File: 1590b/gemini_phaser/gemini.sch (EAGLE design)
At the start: 64 parts, among them IC1 TL074, IC2 TL072, Q1 2N5457, Q2 2N5457, Q3 2N5087, Q4 2N5457, Q5 J112, Q6 2N5457

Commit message: prettified schematics a bit
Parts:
- removed D4: LEDA, diodes:LEDA
- removed R2: 4k7, resistors:R_.3B
- added 9V: DC_MONO, jacks:DC_MONO
- added GND, PAD3: PADRND, supply pins:PADRND
- added IN, OUT: PADSQR, supply pins:PADSQR
- D2: value LEDA -> 5.1vZ; device diodes:LEDA -> diodes:ZENER.3
- D3: value 5.1vZ -> LEDA; device diodes:ZENER.3 -> diodes:LEDA
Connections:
- removed net +9V: D1.A
- removed net N$14: D2.A, R2.1
- new net LS: D3.C, PAD3.P$1
- new net N$34: 9V.TIP, D1.A
- net GND: now also 9V.SLEEVE, D2.A; no longer D2.C, D3.A, D4.C
- net IN: now also IN.P$1
- net N$17: now also D3.A; no longer D4.A
- net N$18: no longer R2.2
- net OUT: now also OUT.P$1
- net VA: now also D2.C; no longer D3.C
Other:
- moved on the sheet: BIAS, C1, C10, C12, C2, C3, C5, C6, C7, C8, D1, DEPTH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

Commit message: convert bitmap logos to polygons
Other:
- moved on the sheet: C4, IC2_A, R1, R3, R7
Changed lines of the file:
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@@
 <setting verticaltext="up"/>
 </settings>
-<grid distance="0.05" unitdist="inch" unit="inch" style="lines" multiple="2" display="no" altdistance="0.01" altunitdist="inch" altunit="inch"/>
+<grid distance="0.1" unitdist="inch" unit="inch" style="lines" multiple="1" display="no" altdistance="0.01" altunitdist="inch" altunit="inch"/>
 <layers>
 <layer number="1" name="Top" color="4" fill="1" visible="no" active="no"/>
@@
 </plain>
 <instances>
-<instance part="R3" gate="G$1" x="55.88" y="86.36"/>
-<instance part="C4" gate="G$1" x="68.58" y="86.36"/>
-<instance part="IC2" gate="_A" x="86.36" y="83.82"/>
+<instance part="R3" gate="G$1" x="53.34" y="86.36"/>
+<instance part="C4" gate="G$1" x="66.04" y="86.36"/>
+<instance part="IC2" gate="_A" x="83.82" y="83.82"/>
 <instance part="IC2" gate="_B" x="208.28" y="116.84" rot="R180"/>
 <instance part="IC2" gate="_PWR" x="55.88" y="127" rot="R180"/>
-<instance part="R7" gate="G$1" x="76.2" y="96.52" rot="R90"/>
+<instance part="R7" gate="G$1" x="73.66" y="96.52" rot="R90"/>
 <instance part="R10" gate="G$1" x="104.14" y="93.98"/>
 <instance part="MIX" gate="G$1" x="111.76" y="83.82" rot="MR180"/>
@@
 <instance part="GND3" gate="GND" x="38.1" y="116.84"/>
 <instance part="R31" gate="G$1" x="233.68" y="106.68" rot="R90"/>
-<instance part="R1" gate="G$1" x="45.72" y="78.74" rot="R90"/>
-<instance part="GND1" gate="GND" x="45.72" y="71.12"/>
+<instance part="R1" gate="G$1" x="43.18" y="78.74" rot="R90"/>
+<instance part="GND1" gate="GND" x="43.18" y="71.12"/>
 <instance part="MODE" gate="1" x="130.81" y="60.96" rot="R270"/>
 <instance part="DEPTH" gate="G$1" x="111.76" y="127" rot="MR90"/>
 <instance part="9V" gate="DC" x="17.78" y="132.08"/>
 <instance part="GND2" gate="GND" x="22.86" y="127"/>
-<instance part="IN" gate="G$1" x="38.1" y="86.36"/>
+<instance part="IN" gate="G$1" x="35.56" y="86.36"/>
 <instance part="OUT" gate="G$1" x="163.83" y="83.82"/>
 <instance part="PAD3" gate="G$1" x="134.62" y="127"/>
@@
 <segment>
 <pinref part="R3" gate="G$1" pin="2"/>
-<wire x1="60.96" y1="86.36" x2="64.77" y2="86.36" width="0.1524" layer="91"/>
+<wire x1="58.42" y1="86.36" x2="62.23" y2="86.36" width="0.1524" layer="91"/>
 <pinref part="C4" gate="G$1" pin="2"/>
 </segment>
@@
 <pinref part="IC2" gate="_A" pin="+IN"/>
 <pinref part="R7" gate="G$1" pin="1"/>
-<wire x1="72.39" y1="86.36" x2="76.2" y2="86.36" width="0.1524" layer="91"/>
-<wire x1="76.2" y1="86.36" x2="78.74" y2="86.36" width="0.1524" layer="91"/>
-<wire x1="76.2" y1="91.44" x2="76.2" y2="86.36" width="0.1524" layer="91"/>
-<junction x="76.2" y="86.36"/>
+<wire x1="69.85" y1="86.36" x2="73.66" y2="86.36" width="0.1524" layer="91"/>
+<wire x1="73.66" y1="86.36" x2="76.2" y2="86.36" width="0.1524" layer="91"/>
+<wire x1="73.66" y1="91.44" x2="73.66" y2="86.36" width="0.1524" layer="91"/>
+<junction x="73.66" y="86.36"/>
 <pinref part="C4" gate="G$1" pin="1"/>
 </segment>
@@
 <segment>
 <pinref part="IC2" gate="_A" pin="OUT"/>
-<wire x1="93.98" y1="83.82" x2="96.52" y2="83.82" width="0.1524" layer="91"/>
+<wire x1="91.44" y1="83.82" x2="96.52" y2="83.82" width="0.1524" layer="91"/>
 <wire x1="96.52" y1="83.82" x2="96.52" y2="93.98" width="0.1524" layer="91"/>
 <pinref part="R10" gate="G$1" pin="1"/>
@@
 <wire x1="55.88" y1="25.4" x2="59.69" y2="25.4" width="0.1524" layer="91"/>
 <pinref part="C2" gate="G$1" pin="2"/>
-<wire x1="96.52" y1="73.66" x2="76.2" y2="73.66" width="0.1524" layer="91"/>
-<wire x1="76.2" y1="73.66" x2="55.88" y2="73.66" width="0.1524" layer="91"/>
+<wire x1="96.52" y1="73.66" x2="73.66" y2="73.66" width="0.1524" layer="91"/>
+<wire x1="73.66" y1="73.66" x2="55.88" y2="73.66" width="0.1524" layer="91"/>
 <wire x1="55.88" y1="73.66" x2="55.88" y2="35.56" width="0.1524" layer="91"/>
 <junction x="55.88" y="35.56"/>
 <pinref part="IC2" gate="_A" pin="-IN"/>
-<wire x1="78.74" y1="81.28" x2="76.2" y2="81.28" width="0.1524" layer="91"/>
-<wire x1="76.2" y1="81.28" x2="76.2" y2="73.66" width="0.1524" layer="91"/>
-<junction x="76.2" y="73.66"/>
+<wire x1="76.2" y1="81.28" x2="73.66" y2="81.28" width="0.1524" layer="91"/>
+<wire x1="73.66" y1="81.28" x2="73.66" y2="73.66" width="0.1524" layer="91"/>
+<junction x="73.66" y="73.66"/>
 </segment>
 </net>
@@
 <segment>
 <pinref part="R3" gate="G$1" pin="1"/>
-<wire x1="35.56" y1="86.36" x2="38.1" y2="86.36" width="0.1524" layer="91"/>
+<wire x1="27.94" y1="86.36" x2="35.56" y2="86.36" width="0.1524" layer="91"/>
 <pinref part="R1" gate="G$1" pin="2"/>
-<wire x1="38.1" y1="86.36" x2="45.72" y2="86.36" width="0.1524" layer="91"/>
-<wire x1="45.72" y1="86.36" x2="50.8" y2="86.36" width="0.1524" layer="91"/>
-<wire x1="45.72" y1="83.82" x2="45.72" y2="86.36" width="0.1524" layer="91"/>
-<junction x="45.72" y="86.36"/>
-<label x="35.56" y="86.36" size="1.778" layer="95" rot="R180" xref="yes"/>
+<wire x1="35.56" y1="86.36" x2="43.18" y2="86.36" width="0.1524" layer="91"/>
+<wire x1="43.18" y1="86.36" x2="48.26" y2="86.36" width="0.1524" layer="91"/>
+<wire x1="43.18" y1="83.82" x2="43.18" y2="86.36" width="0.1524" layer="91"/>
+<junction x="43.18" y="86.36"/>
+<label x="27.94" y="86.36" size="1.778" layer="95" rot="R180" xref="yes"/>
 <pinref part="IN" gate="G$1" pin="P$1"/>
-<junction x="38.1" y="86.36"/>
+<junction x="35.56" y="86.36"/>
 </segment>
 </net>
@@
 <wire x1="153.67" y1="83.82" x2="154.94" y2="83.82" width="0.1524" layer="91"/>
 <wire x1="154.94" y1="83.82" x2="163.83" y2="83.82" width="0.1524" layer="91"/>
-<wire x1="163.83" y1="83.82" x2="166.37" y2="83.82" width="0.1524" layer="91"/>
+<wire x1="163.83" y1="83.82" x2="171.45" y2="83.82" width="0.1524" layer="91"/>
 <wire x1="154.94" y1="81.28" x2="154.94" y2="83.82" width="0.1524" layer="91"/>
 <junction x="154.94" y="83.82"/>
 <pinref part="C9" gate="G$1" pin="1"/>
-<label x="166.37" y="83.82" size="1.778" layer="95" xref="yes"/>
+<label x="171.45" y="83.82" size="1.778" layer="95" xref="yes"/>
 <pinref part="OUT" gate="G$1" pin="P$1"/>
 <junction x="163.83" y="83.82"/>
@@
 <segment>
 <pinref part="R7" gate="G$1" pin="2"/>
-<wire x1="76.2" y1="101.6" x2="76.2" y2="102.87" width="0.1524" layer="91"/>
-<label x="76.2" y="102.87" size="1.778" layer="95" rot="R90" xref="yes"/>
-</segment>
-<segment>
+<wire x1="73.66" y1="101.6" x2="73.66" y2="102.87" width="0.1524" layer="91"/>
+<label x="73.66" y="102.87" size="1.778" layer="95" rot="R90" xref="yes"/>
+</segment>
+<segment>

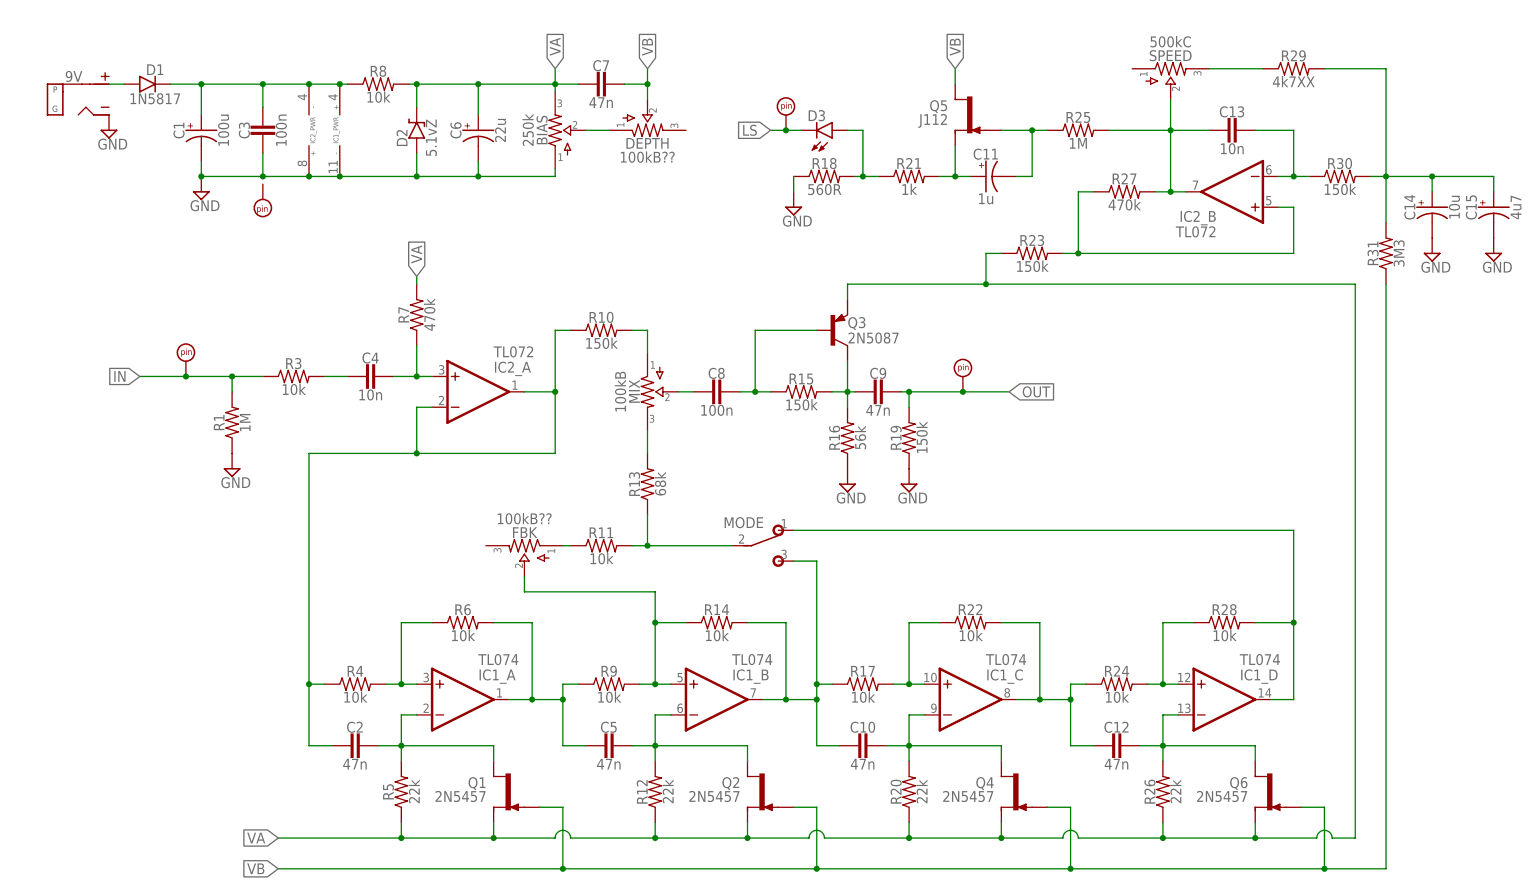
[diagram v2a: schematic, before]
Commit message: add SIREN build doc
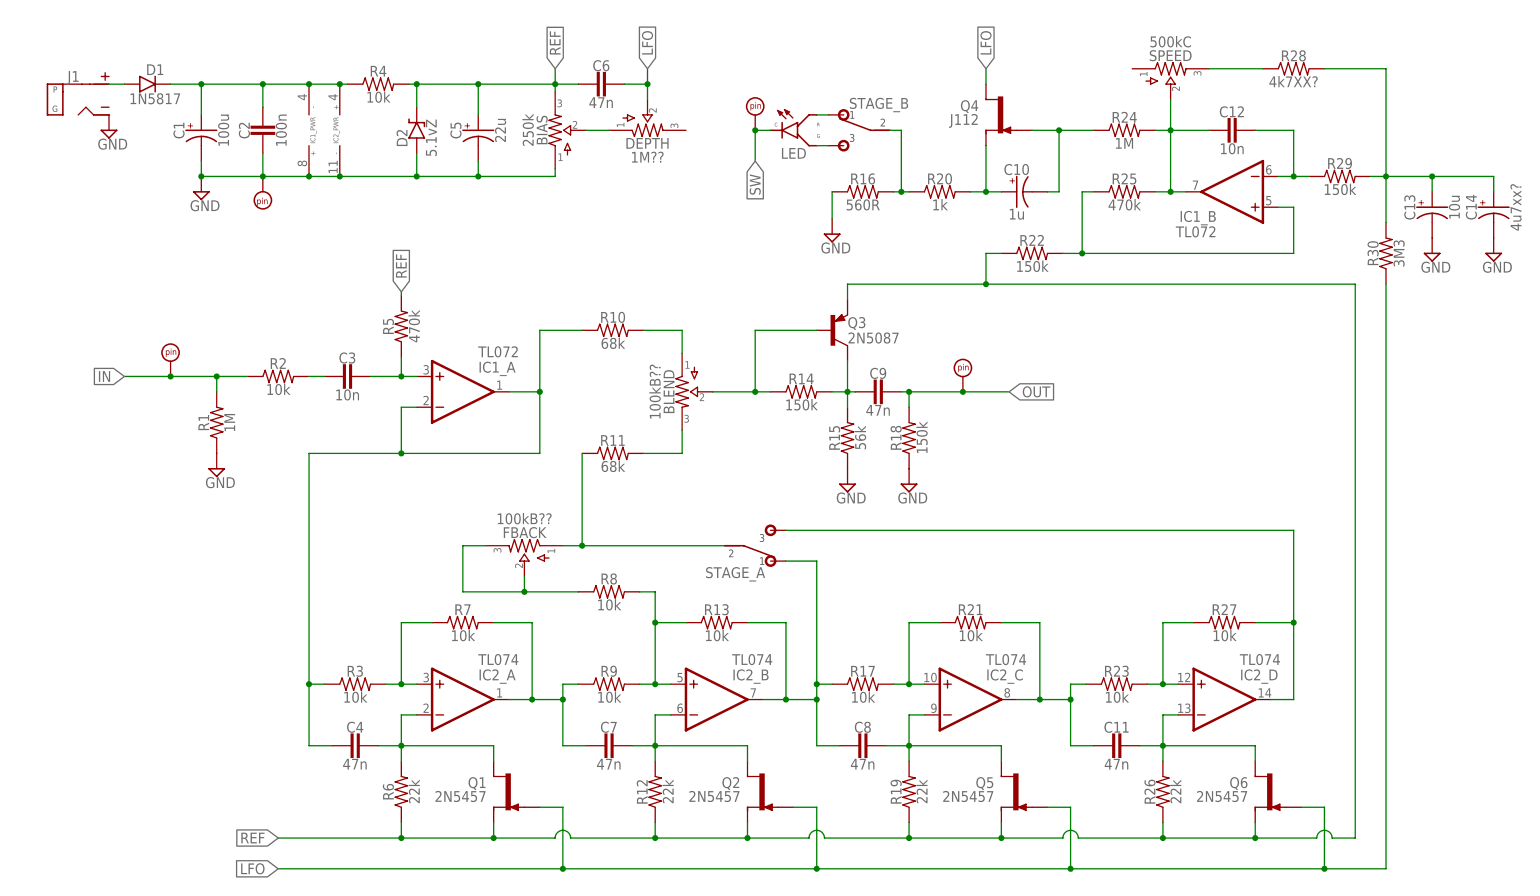
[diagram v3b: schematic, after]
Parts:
- removed C15: 4u7, capacitors-elec:0501
- removed D3: LEDA, diodes:LEDA
- removed GND: PADRND, supply pins:PADRND
- removed IN: PADSQR, supply pins:PADSQR
- removed MIX: 100kB, potentiometers:POTS16MM
- removed MODE: (no value), switches:SPDTPADS
- removed R31: 3M3, resistors:R_.3B
- added BLEND: 100kB??, potentiometers:POTS16MM
- added LED: LED_DUAL, diodes:LED_DUAL
- added PAD1: PADSQR, supply pins:PADSQR
- added PAD2: PADRND, supply pins:PADRND
- added R2: 10k, resistors:R_.3B
- added STAGE: (no value), switches:DPDTPCB
- C10: value 47n -> 1u; device capacitors-film:CER/FILM2 -> capacitors-elec:0501
- C11: value 1u -> 47n; device capacitors-elec:0501 -> capacitors-film:CER/FILM2
- C12: value 47n -> 10n
- C13: value 10n -> 10u; device capacitors-film:CER/FILM2 -> capacitors-elec:0501
- C14: value 10u -> 4u7xx?
- C2: value 47n -> 100n
- C3: value 100n -> 10n
- C4: value 10n -> 47n
- C5: value 47n -> 22u; device capacitors-film:CER/FILM2 -> capacitors-elec:0501
- C6: value 22u -> 47n; device capacitors-elec:0501 -> capacitors-film:CER/FILM2
- C8: value 100n -> 47n
- DEPTH: value 100kB?? -> 1M??
- IC1: value TL074 -> TL072; device integrated circuits:QUADTH -> integrated circuits:DUALTH
- IC2: value TL072 -> TL074; device integrated circuits:DUALTH -> integrated circuits:QUADTH
- Q4: value 2N5457 -> J112; device transistors:2N5457 -> transistors:J201
- Q5: value J112 -> 2N5457; device transistors:J201 -> transistors:2N5457
- R10: value 150k -> 68k
- R11: value 10k -> 68k
- R13: value 68k -> 10k
- R14, R22: value 10k -> 150k
- R15: value 150k -> 56k
- R16: value 56k -> 560R
- R18: value 560R -> 150k
- R19: value 150k -> 22k
- R20: value 22k -> 1k
- R21: value 1k -> 10k
- R23: value 150k -> 10k
- R24: value 10k -> 1M
- R25: value 1M -> 470k
- R27, R7: value 470k -> 10k
- R28: value 10k -> 4k7XX?
- R29: value 4k7XX -> 150k
- R30: value 150k -> 3M3
- R5: value 22k -> 470k
- R6: value 10k -> 22k
- renumbered 9V to J1, FBK to FBACK, OUT to PAD4
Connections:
- removed net LS: D3.C, PAD3.P$1
- removed net N$5: C8.2, MIX.2
- removed net VA: BIAS.3, C6.+, C7.2, D2.C, Q1.S, Q2.S, Q3.E, Q4.S, Q6.S, R12.1, R20.1, R23.1, R26.1, R5.1, R7.2, R8.2
- removed net VB: C7.1, DEPTH.2, Q1.G, Q2.G, Q4.G, Q5.D, Q6.G, R31.1
- new net LED: LED.G, STAGE_B.3
- new net LFO: C6.1, DEPTH.2, Q1.G, Q2.G, Q4.D, Q5.G, Q6.G, R30.1
- new net N$35: LED.R, STAGE_B.1
- new net REF: BIAS.3, C5.+, C6.2, D2.C, Q1.S, Q2.S, Q3.E, Q5.S, Q6.S, R12.1, R19.1, R22.1, R26.1, R4.2, R5.2, R6.1
- new net SW: LED.C, PAD3.P$1
- net GND: now also C13.-, C2.2, C5.-, IC1_PWR.V+, IC2_PWR.V-, PAD2.P$1, R15.1; no longer C15.-, C3.2, C6.-, IC1_PWR.V-, IC2_PWR.V+, R19.1
- net IN: now also PAD1.P$1, R2.1; no longer IN.P$1, R3.1
- net N$1: now also C3.2, R2.2; no longer C4.2, R3.2
- net N$10: now also IC1_B.+IN, R22.2, R25.1; no longer IC2_B.+IN, R23.2, R27.1
- net N$11: now also C12.2, IC1_B.OUT, R24.2; no longer C13.2, IC2_B.OUT, R27.2
- net N$12: now also R28.1; no longer R29.1
- net N$13: now also C12.1, IC1_B.-IN, R29.1; no longer C13.1, IC2_B.-IN, R30.1
- net N$15: now also C10.-, Q4.G, R24.1; no longer C11.-, Q5.G, R25.1
- net N$16: now also C10.+, Q4.S, R20.2; no longer C11.+, Q5.S, R21.2
- net N$17: now also R16.2, R20.1, STAGE_B.2; no longer D3.A, R18.2, R21.1
- net N$18: now also C2.1, IC1_PWR.V-, IC2_PWR.V+, R4.1; no longer C3.1, IC1_PWR.V+, IC2_PWR.V-, R8.1
- net N$19: now also BLEND.3, R11.2; no longer FBACK.1, R11.1
- net N$2: now also C3.1, IC1_A.+IN, R5.1; no longer C4.1, IC2_A.+IN, R7.1
- net N$20: now also IC2_B.+IN, R13.1, R8.2; no longer FBACK.2, IC1_B.+IN, R14.1
- net N$21: now also C4.1, IC2_A.-IN, R6.2; no longer C2.1, IC1_A.-IN, R5.2
- net N$22: now also IC2_A.+IN, R3.2, R7.1; no longer IC1_A.+IN, R4.2, R6.1
- net N$23: now also C7.2, IC2_A.OUT, R7.2; no longer C5.2, IC1_A.OUT, R6.2
- net N$24: now also C7.1, IC2_B.-IN; no longer C5.1, IC1_B.-IN
- net N$25: now also IC2_D.OUT, R27.2, STAGE_A.3; no longer IC1_D.OUT, MODE.O, R28.2
- net N$26: now also C8.2, IC2_B.OUT, R13.2, STAGE_A.1; no longer C10.2, IC1_B.OUT, MODE.S, R14.2
- net N$27: now also C8.1, IC2_C.-IN, Q5.D, R19.2; no longer C10.1, IC1_C.-IN, Q4.D, R20.2
- net N$28: now also IC2_C.+IN, R21.1; no longer IC1_C.+IN, R22.1
- net N$29: now also C11.2, IC2_C.OUT, R21.2, R23.1; no longer C12.2, IC1_C.OUT, R22.2, R24.1
- net N$3: now also C4.2, IC1_A.-IN, IC1_A.OUT, R3.1; no longer C2.2, IC2_A.-IN, IC2_A.OUT, R4.1
- net N$30: now also C11.1, IC2_D.-IN; no longer C12.1, IC1_D.-IN
- net N$31: now also IC2_D.+IN, R23.2, R27.1; no longer IC1_D.+IN, R24.2, R28.1
- net N$32: now also FBACK.1, R11.1, STAGE_A.2; no longer MODE.P, R11.2, R13.1
- net N$4: now also BLEND.1; no longer MIX.1
- net N$6: now also BLEND.2, R14.1; no longer C8.1, R15.1
- net N$7: now also R14.2; no longer R16.2
- net N$8: now also FBACK.2, FBACK.3, R8.1; no longer MIX.3, R13.2
- net N$9: now also C13.+, R28.2; no longer C15.+, R31.2
- net OUT: now also R18.2; no longer R19.2
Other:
- moved on the sheet: C12, C14, C2, C3, C4, C7, C8, IC1_A, IC1_B, IC1_PWR, IC2_A, IC2_B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
